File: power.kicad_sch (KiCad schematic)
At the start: 13 parts, among them J1 USB_B_Micro, U2 S2B-PH-K-S-GW, U3 AP2112K-3.3TRG1, U4 MCP73831T-2ACI/OT, U6 MSK-12C02_SMD_SPDT_SWITCH

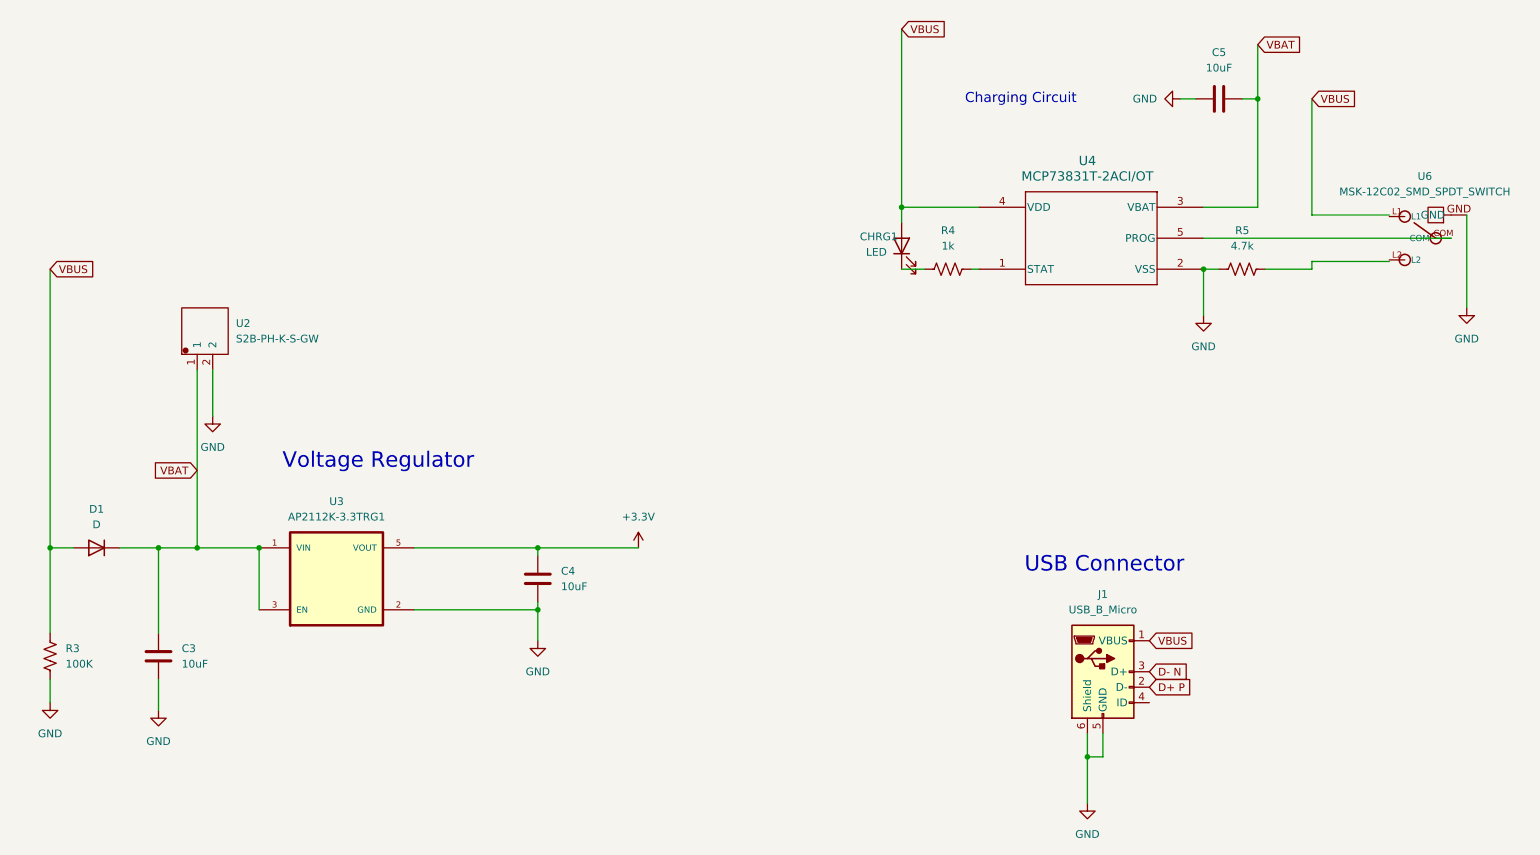
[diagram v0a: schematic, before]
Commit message: Condense schematic
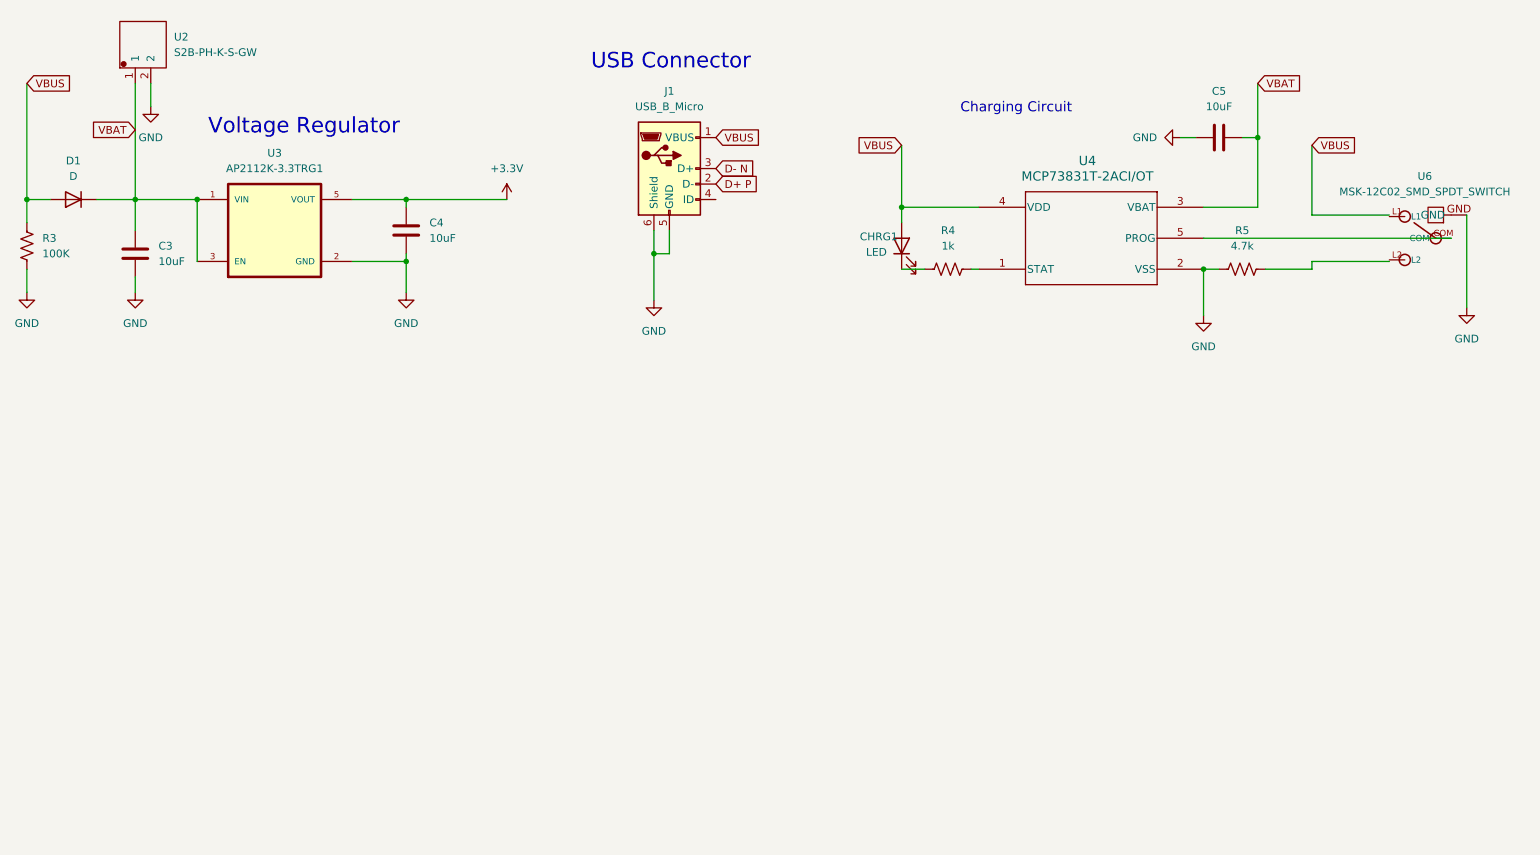
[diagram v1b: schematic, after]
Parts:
- C3, C4, C5: footprint Capacitor_SMD:C_0603_1608Metric -> Capacitor_SMD:C_0402_1005Metric
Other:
- moved on the sheet: C3, C4, C5, D1, J1, R3, U2, U3

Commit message: PCB Smol Time
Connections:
- net VBUS: now also U6.L1
- net at U6.L2: now also R5.2
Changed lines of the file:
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@@
+	)
+	(junction
+		(at 252.73 64.516)
+		(diameter 0)
+		(color 0 0 0 0)
 	)
 	(junction
@@
 	)
 	(junction
+		(at 252.73 57.404)
+		(diameter 0)
+		(color 0 0 0 0)
+	)
+	(junction
 		(at 91.44 54.61)
 		(diameter 0)
@@
 	(wire
 		(pts
+			(xy 252.73 55.88) (xy 252.73 57.404)
+		)
+		(stroke
+			(width 0)
+			(type default)
+		)
+	)
+	(wire
+		(pts
 			(xy 33.02 54.61) (xy 29.21 54.61)
 		)
@@
 	(wire
 		(pts
-			(xy 240.03 66.04) (xy 232.41 66.04)
-		)
-		(stroke
-			(width 0)
-			(type default)
-		)
-	)
-	(wire
-		(pts
-			(xy 240.03 64.77) (xy 240.03 66.04)
+			(xy 238.76 66.04) (xy 232.41 66.04)
+		)
+		(stroke
+			(width 0)
+			(type default)
+		)
+	)
+	(wire
+		(pts
+			(xy 238.76 64.77) (xy 238.76 66.04)
 		)
 		(stroke
@@
 	(wire
 		(pts
-			(xy 240.03 57.15) (xy 252.73 57.15)
+			(xy 240.03 55.88) (xy 252.73 55.88)
+		)
+		(stroke
+			(width 0)
+			(type default)
+		)
+	)
+	(wire
+		(pts
+			(xy 252.73 57.404) (xy 252.73 58.42)
 		)
 		(stroke
@@
 	(wire
 		(pts
+			(xy 252.73 63.5) (xy 252.73 64.516)
+		)
+		(stroke
+			(width 0)
+			(type default)
+		)
+	)
+	(wire
+		(pts
 			(xy 91.44 64.77) (xy 91.44 69.85)
 		)
@@
 	(wire
 		(pts
-			(xy 240.03 64.77) (xy 252.73 64.77)
+			(xy 238.76 64.77) (xy 252.73 64.77)
 		)
 		(stroke
@@
 	(wire
 		(pts
-			(xy 240.03 45.72) (xy 240.03 57.15)
+			(xy 240.03 45.72) (xy 240.03 55.88)
 		)
 		(stroke
@@
 		)
 		(stroke
+			(width 0)
+			(type default)
+		)
+	)
+	(wire
+		(pts
+			(xy 252.73 64.516) (xy 252.73 64.77)
+		)
+		(stroke

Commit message: update power circuit
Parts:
- added D2: D, Diode_SMD:D_0603_1608Metric, symbol uSlime:D
- added R6: 180Ω, Resistor_SMD:R_0402_1005Metric, symbol uSlime:R_US
- R3: value 100K -> 180Ω
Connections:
- net D+ P: now also J1.3 (D+); no longer J1.2 (D-)
- net D- N: now also J1.2 (D-); no longer J1.3 (D+)
- net GND: now also R6.2; no longer R3.2
- net VBAT: now also R3.1, D2.2 (A); no longer C3.1, D1.1 (K), U3.1 (VIN), U3.3 (EN)
- net VBUS: no longer R3.1
- new net: C3.1, D1.1 (K), D2.1 (K), U3.1 (VIN), U3.3 (EN)
- new net batSens: R3.2, R6.1
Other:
- moved on the sheet: C3, C4, D1, U2, U3

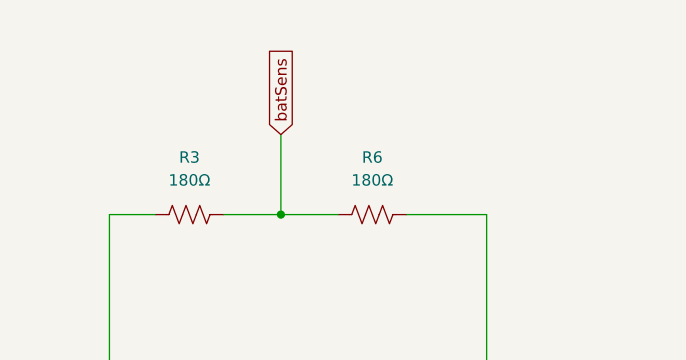
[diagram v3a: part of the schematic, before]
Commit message: update battery sense
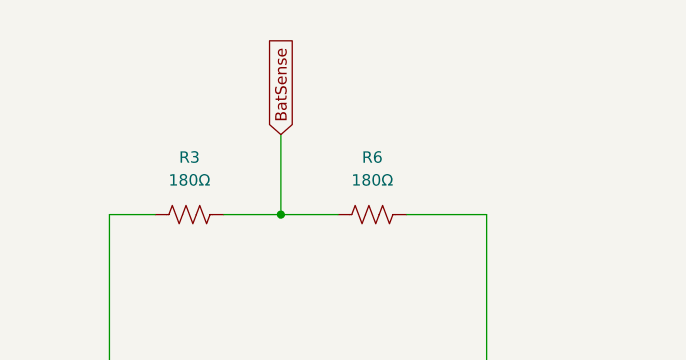
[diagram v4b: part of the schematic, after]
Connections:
- net batSens renamed BatSense
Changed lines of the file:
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@@
 		)
 	)
-	(global_label "batSens"
+	(global_label "BatSense"
 		(shape input)
 		(at 58.42 36.83 90)
@@
 		)
 		(property "Intersheetrefs" "${INTERSHEET_REFS}"
-			(at 58.42 26.3459 90)
+			(at 58.42 25.1363 90)
 			(effects
 				(font

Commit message: Update power.kicad_sch
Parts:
- removed R6: 180Ω, Resistor_SMD:R_0402_1005Metric, symbol uSlime:R_US
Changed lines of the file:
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@@
-	)
-	(junction
-		(at 49.53 80.01)
-		(diameter 0)
-		(color 0 0 0 0)
-	)
-	(junction
-		(at 58.42 45.72)
-		(diameter 0)
-		(color 0 0 0 0)
 	)
 	(junction
@@
 	(wire
 		(pts
-			(xy 72.39 45.72) (xy 81.28 45.72)
-		)
-		(stroke
-			(width 0)
-			(type default)
-		)
-	)
-	(wire
-		(pts
 			(xy 238.76 64.77) (xy 238.76 66.04)
 		)
@@
 	(wire
 		(pts
-			(xy 81.28 45.72) (xy 81.28 80.01)
-		)
-		(stroke
-			(width 0)
-			(type default)
-		)
-	)
-	(wire
-		(pts
 			(xy 240.03 55.88) (xy 252.73 55.88)
 		)
@@
 	(wire
 		(pts
-			(xy 81.28 80.01) (xy 49.53 80.01)
-		)
-		(stroke
-			(width 0)
-			(type default)
-		)
-	)
-	(wire
-		(pts
 			(xy 82.55 109.22) (xy 91.44 109.22)
 		)
@@
 		(pts
 			(xy 46.99 96.52) (xy 46.99 99.06)
-		)
-		(stroke
-			(width 0)
-			(type default)
-		)
-	)
-	(wire
-		(pts
-			(xy 58.42 45.72) (xy 64.77 45.72)
 		)
 		(stroke
@@
 					(unit 1)
 				)
-			)
-		)
-	)
-	(symbol
-		(lib_id "uSlime:R_US")
-		(at 68.58 45.72 90)
-		(unit 1)
-		(exclude_from_sim no)
-		(in_bom yes)
-		(on_board yes)
-		(dnp no)
-		(fields_autoplaced yes)
-		(property "Reference" "R6"
-			(at 68.58 39.37 90)
-			(effects
-				(font
-					(size 1.27 1.27)
-				)
-			)
-		)
-		(property "Value" "180Ω"
-			(at 68.58 41.91 90)
-			(effects
-				(font
-					(size 1.27 1.27)
-				)
-			)
-		)
-		(property "Footprint" "Resistor_SMD:R_0402_1005Metric"
-			(at 68.834 44.704 90)
-			(effects
-				(font
-					(size 1.27 1.27)
-				)
-				(hide yes)
-			)
-		)
-		(property "Datasheet" "~"
-			(at 68.58 45.72 0)
-			(effects
-				(font
-					(size 1.27 1.27)
-				)
-				(hide yes)
-			)
-		)
-		(property "Description" "Resistor, US symbol"
-			(at 68.58 45.72 0)
-			(effects
-				(font
-					(size 1.27 1.27)
-				)
-				(hide yes)
-			)
-		)
-		(pin "2"
-		)
-		(pin "1"
-		)
-		(instances
-			(project "uSlime"
-				(path "/f32c1c49-f803-4e7c-a530-6db148a7ba36/9141278c-15a6-43aa-8c9d-f1bdf7efadba"
-					(reference "R6")
-					(unit 1)
-				)

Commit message: Create prelim PCB
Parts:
- removed J1: USB_B_Micro, Connector_USB:USB_Micro-B_Amphenol_10103594-0001LF_Horizontal, symbol uSlime:USB_B_Micro
- removed U2: S2B-PH-K-S-GW, Connector_JST:JST_PH_S2B-PH-K_1x02_P2.00mm_Horizontal, symbol uSlime:S2B-PH-K-S-GW
- added CN2: 1.25T-2AW, uSlime-libs:CONN-TH_2P-P1.25_1.25T-2AW, symbol uSlime:1.25T-2AW
- added J1: USB_C_Receptacle_USB2.0_14P, Connector_USB:USB_C_Receptacle_GCT_USB4105-xx-A_16P_TopMnt_Horizontal, symbol uSlime:USB_C_Receptacle_USB2.0_14P
- added R6, R7: 5.1k, Resistor_SMD:R_0402_1005Metric, symbol uSlime:R_US
- D1, D2: footprint Diode_SMD:D_0603_1608Metric -> Diode_SMD:D_0402_1005Metric
- R3: value 180Ω -> 180k
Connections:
- net D+ P: now also J1.A6 (D+), J1.B6 (D+)
- net D- N: now also J1.A7 (D-), J1.B7 (D-)
- net GND: now also CN2.2, J1.A1 (GND), J1.A12 (GND), J1.B1 (GND), J1.B12 (GND), J1.S1 (SHIELD), R6.1, R7.1
- net VBAT: now also CN2.1
- net VBUS: now also J1.A4 (VBUS), J1.A9 (VBUS), J1.B4 (VBUS), J1.B9 (VBUS)
- new net: J1.A5 (CC1), R7.2
- new net: J1.B5 (CC2), R6.2
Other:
- moved on the sheet: C3, C4, C5, CHRG1, D1, D2, R3, R4, R5, U3, U4, U6

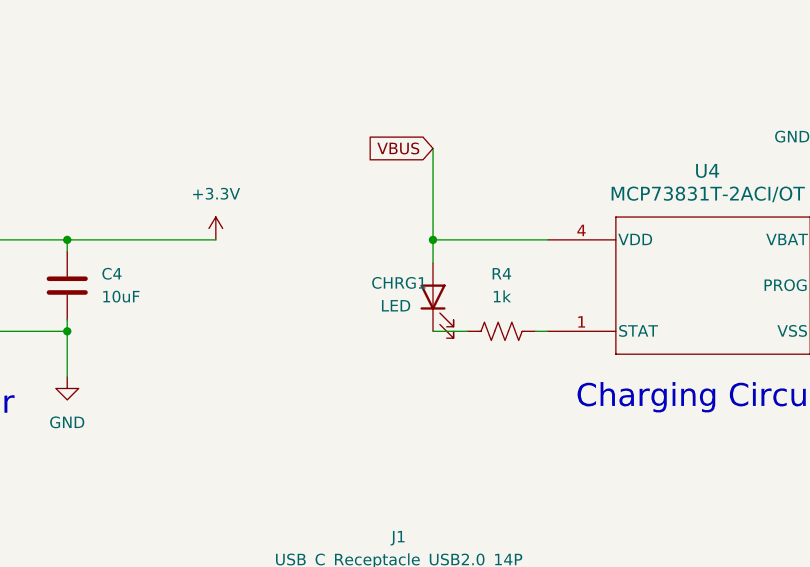
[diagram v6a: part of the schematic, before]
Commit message: 2nd version but smaller at 25x28
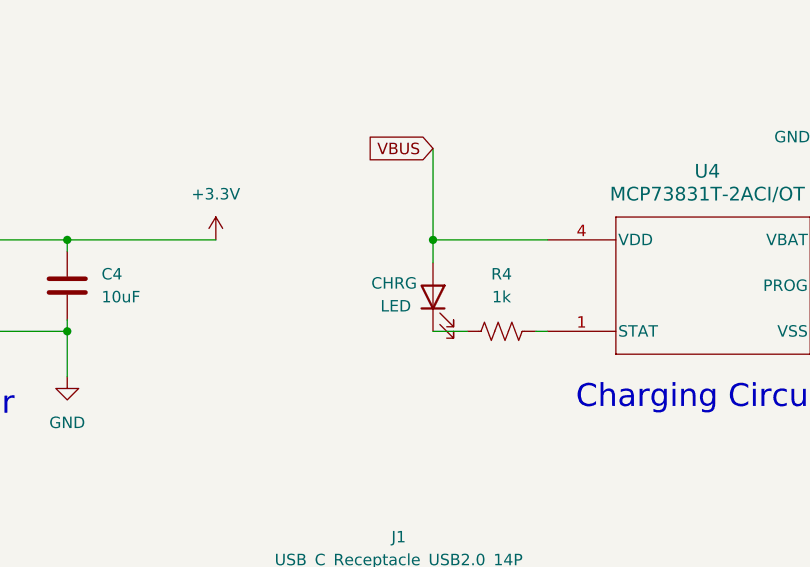
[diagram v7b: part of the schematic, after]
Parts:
- renumbered CHRG1 to CHRG
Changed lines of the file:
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@@
 		(on_board yes)
 		(dnp no)
-		(property "Reference" "CHRG1"
+		(property "Reference" "CHRG"
 			(at 145.542 82.296 90)
 			(effects
@@
 			(project "uSlime"
 				(path "/f32c1c49-f803-4e7c-a530-6db148a7ba36/9141278c-15a6-43aa-8c9d-f1bdf7efadba"
-					(reference "CHRG1")
+					(reference "CHRG")
 					(unit 1)
 				)

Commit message: Add logo and remove crystal
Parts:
- added TP5: 3.3V, TestPoint:TestPoint_Pad_2.0x2.0mm, symbol uSlime:TestPoint
- added TP6: GND, TestPoint:TestPoint_Pad_2.0x2.0mm, symbol uSlime:TestPoint
- renumbered CHRG to CHRG1
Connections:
- net +3.3V: now also TP5.1
- net GND: now also TP6.1
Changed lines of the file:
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@@
+	)
+	(junction
+		(at 128.27 77.47)
+		(diameter 0)
+		(color 0 0 0 0)
 	)
 	(junction
@@
 		(on_board yes)
 		(dnp no)
-		(property "Reference" "CHRG"
+		(property "Reference" "CHRG1"
 			(at 145.542 82.296 90)
 			(effects
@@
 			(project "uSlime"
 				(path "/f32c1c49-f803-4e7c-a530-6db148a7ba36/9141278c-15a6-43aa-8c9d-f1bdf7efadba"
-					(reference "CHRG")
+					(reference "CHRG1")
 					(unit 1)
 				)
@@
 					(unit 1)
 				)
+			)
+		)
+	)
+	(symbol
+		(lib_id "uSlime:TestPoint")
+		(at 128.27 77.47 270)
+		(unit 1)
+		(exclude_from_sim no)
+		(in_bom yes)
+		(on_board yes)
+		(dnp no)
+		(property "Reference" "TP5"
+			(at 133.096 77.47 90)
+			(effects
+				(font
+					(size 1.27 1.27)
+				)
+				(justify left)
+			)
+		)
+		(property "Value" "3.3V"
+			(at 136.906 77.47 90)
+			(effects
+				(font
+					(size 1.27 1.27)
+				)
+				(justify left)
+			)
+		)
+		(property "Footprint" "TestPoint:TestPoint_Pad_2.0x2.0mm"
+			(at 128.27 82.55 0)
+			(effects
+				(font
+					(size 1.27 1.27)
+				)
+				(hide yes)
+			)
+		)
+		(property "Datasheet" "~"
+			(at 128.27 82.55 0)
+			(effects
+				(font
+					(size 1.27 1.27)
+				)
+				(hide yes)
+			)
+		)
+		(property "Description" "test point"
+			(at 128.27 77.47 0)
+			(effects
+				(font
+					(size 1.27 1.27)
+				)
+				(hide yes)
+			)
+		)
+		(pin "1"
+		)
+		(instances
+			(project "uSlime"
+				(path "/f32c1c49-f803-4e7c-a530-6db148a7ba36/9141278c-15a6-43aa-8c9d-f1bdf7efadba"
+					(reference "TP5")
+					(unit 1)
+				)
+			)
+		)
+	)
+	(symbol
+		(lib_id "uSlime:TestPoint")
+		(at 111.76 87.63 270)
+		(unit 1)
+		(exclude_from_sim no)
+		(in_bom yes)
+		(on_board yes)
+		(dnp no)
+		(property "Reference" "TP6"
+			(at 116.586 87.63 90)
+			(effects
+				(font
+					(size 1.27 1.27)
+				)
+				(justify left)
+			)
+		)
+		(property "Value" "GND"
+			(at 120.396 87.63 90)
+			(effects
+				(font
+					(size 1.27 1.27)
+				)
+				(justify left)
+			)
+		)
+		(property "Footprint" "TestPoint:TestPoint_Pad_2.0x2.0mm"
+			(at 111.76 92.71 0)
+			(effects
+				(font
+					(size 1.27 1.27)
+				)
+				(hide yes)
+			)
+		)
+		(property "Datasheet" "~"
+			(at 111.76 92.71 0)
+			(effects
+				(font
+					(size 1.27 1.27)
+				)
+				(hide yes)
+			)
+		)
+		(property "Description" "test point"
+			(at 111.76 87.63 0)
+			(effects
+				(font
+					(size 1.27 1.27)
+				)
+				(hide yes)
+			)
+		)
+		(pin "1"
+		)
+		(instances
+			(project "uSlime"
+				(path "/f32c1c49-f803-4e7c-a530-6db148a7ba36/9141278c-15a6-43aa-8c9d-f1bdf7efadba"
+					(reference "TP6")
+					(unit 1)
+				)
